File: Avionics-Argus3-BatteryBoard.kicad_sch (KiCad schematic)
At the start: 6 parts

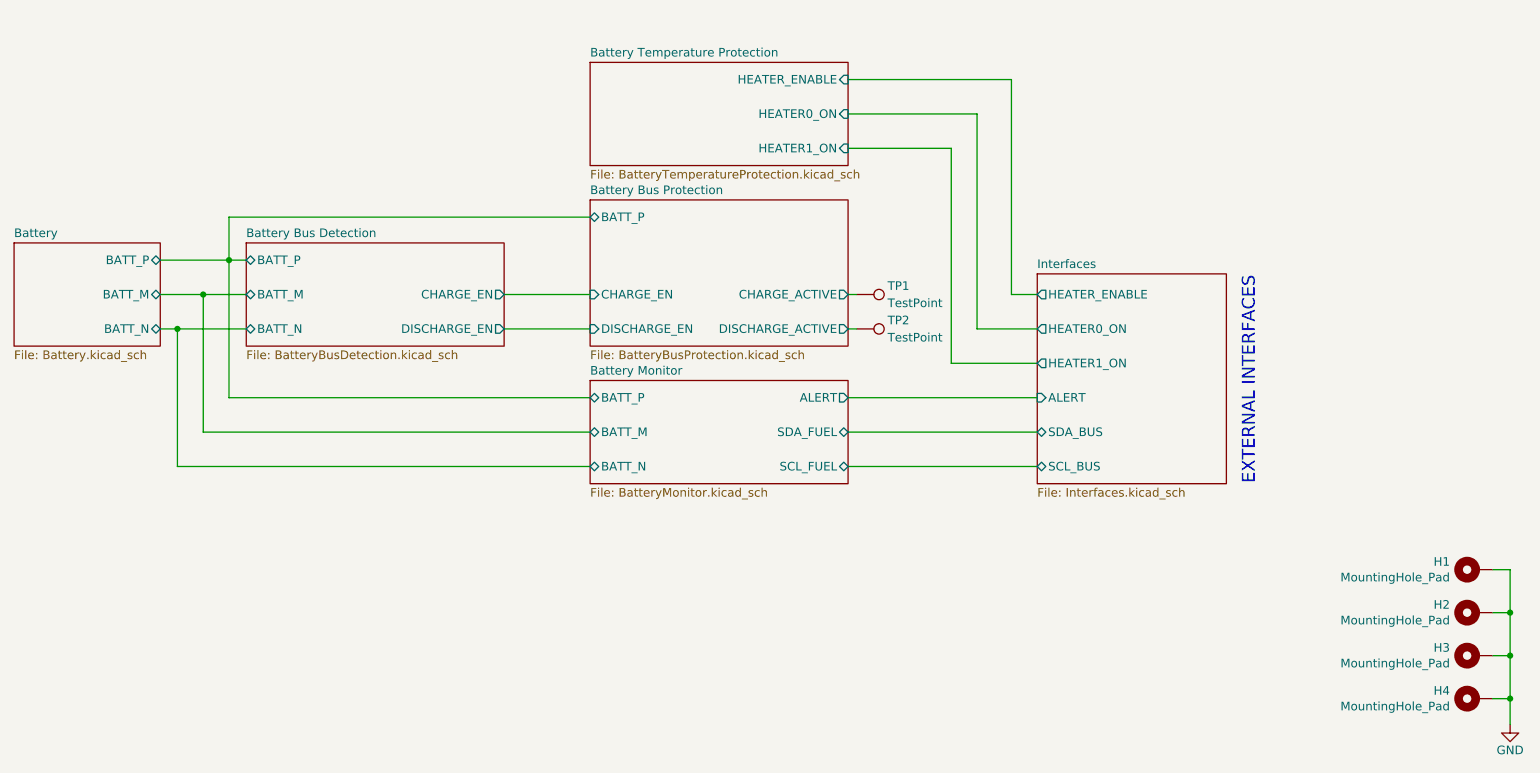
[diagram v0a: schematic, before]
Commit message: Updated Interface to MCU_Subsystem
removed old interface, added STM32U375CE with minimum design components for our operation. Still need to find voltage converter from BATT_P to 3.3v.
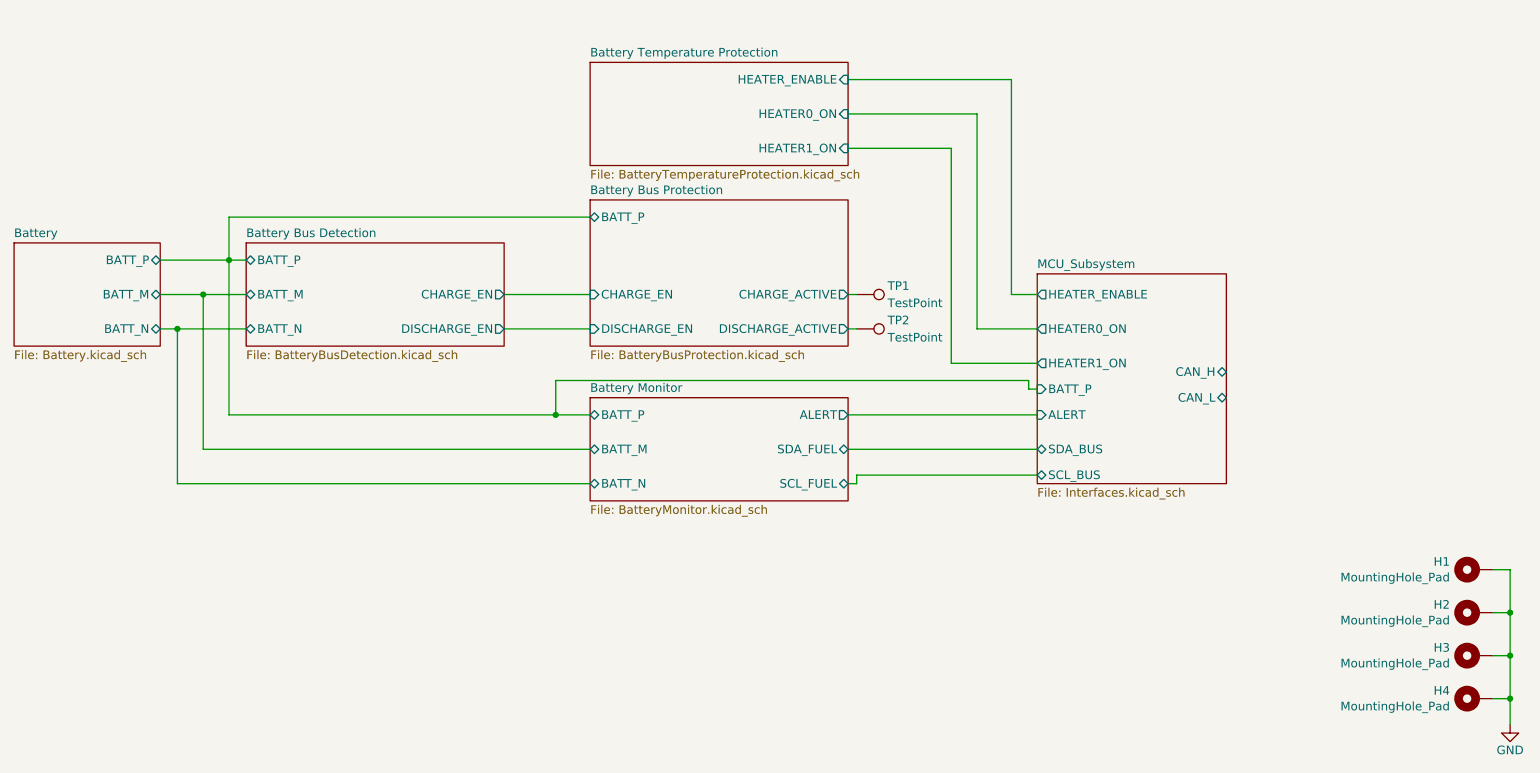
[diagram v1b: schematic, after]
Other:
- sheet Interfaces renamed MCU_Subsystem
- sheet MCU_Subsystem ports: added BATT_P, CAN_H, CAN_L; removed none
- note removed: "EXTERNAL INTERFACES"
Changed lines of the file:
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@@
 		(comment 3 "V. Rajesh")
-	)
-	(text "EXTERNAL INTERFACES"
-		(exclude_from_sim no)
-		(at 216.662 106.68 90)
-		(effects
-			(font
-				(size 1.905 1.905)
-			)
-		)
 	)
 	(junction
@@
 	)
 	(junction
+		(at 114.3 111.76)
+		(diameter 0)
+		(color 0 0 0 0)
+	)
+	(junction
 		(at 62.23 93.98)
 		(diameter 0)
@@
 	(wire
 		(pts
-			(xy 58.42 99.06) (xy 58.42 119.38)
+			(xy 58.42 99.06) (xy 58.42 121.92)
+		)
+		(stroke
+			(width 0)
+			(type default)
+		)
+	)
+	(wire
+		(pts
+			(xy 157.48 116.84) (xy 185.42 116.84)
 		)
 		(stroke
@@
 	(wire
 		(pts
+			(xy 157.48 111.76) (xy 185.42 111.76)
+		)
+		(stroke
+			(width 0)
+			(type default)
+		)
+	)
+	(wire
+		(pts
 			(xy 66.04 82.55) (xy 119.38 82.55)
 		)
@@
 	(wire
 		(pts
-			(xy 62.23 114.3) (xy 119.38 114.3)
+			(xy 62.23 116.84) (xy 119.38 116.84)
 		)
 		(stroke
@@
 	(wire
 		(pts
+			(xy 184.15 107.95) (xy 185.42 107.95)
+		)
+		(stroke
+			(width 0)
+			(type default)
+		)
+	)
+	(wire
+		(pts
 			(xy 106.68 99.06) (xy 119.38 99.06)
 		)
@@
 	(wire
 		(pts
+			(xy 158.75 120.65) (xy 185.42 120.65)
+		)
+		(stroke
+			(width 0)
+			(type default)
+		)
+	)
+	(wire
+		(pts
 			(xy 157.48 99.06) (xy 158.75 99.06)
 		)
@@
 	(wire
 		(pts
+			(xy 114.3 106.68) (xy 114.3 111.76)
+		)
+		(stroke
+			(width 0)
+			(type default)
+		)
+	)
+	(wire
+		(pts
+			(xy 184.15 106.68) (xy 114.3 106.68)
+		)
+		(stroke
+			(width 0)
+			(type default)
+		)
+	)
+	(wire
+		(pts
 			(xy 255.27 147.32) (xy 255.27 153.67)
 		)
@@
 	(wire
 		(pts
-			(xy 157.48 109.22) (xy 185.42 109.22)
-		)
-		(stroke
-			(width 0)
-			(type default)
-		)
-	)
-	(wire
-		(pts
 			(xy 157.48 67.31) (xy 176.53 67.31)
 		)
@@
 	(wire
 		(pts
-			(xy 157.48 114.3) (xy 185.42 114.3)
+			(xy 184.15 107.95) (xy 184.15 106.68)
 		)
 		(stroke
@@
 	(wire
 		(pts
-			(xy 119.38 109.22) (xy 66.04 109.22)
+			(xy 119.38 111.76) (xy 114.3 111.76)
 		)
 		(stroke
@@
 	(wire
 		(pts
-			(xy 66.04 88.9) (xy 66.04 109.22)
+			(xy 66.04 88.9) (xy 66.04 111.76)
 		)
 		(stroke
@@
 	(wire
 		(pts
-			(xy 157.48 119.38) (xy 185.42 119.38)
+			(xy 157.48 121.92) (xy 158.75 121.92)
 		)
 		(stroke
@@
 	(wire
 		(pts
-			(xy 62.23 93.98) (xy 62.23 114.3)
+			(xy 62.23 93.98) (xy 62.23 116.84)
 		)
 		(stroke
@@
 	(wire
 		(pts
+			(xy 158.75 121.92) (xy 158.75 120.65)
+		)
+		(stroke
+			(width 0)
+			(type default)
+		)
+	)
+	(wire
+		(pts
+			(xy 114.3 111.76) (xy 66.04 111.76)
+		)
+		(stroke
+			(width 0)
+			(type default)
+		)
+	)
+	(wire
+		(pts
 			(xy 157.48 93.98) (xy 158.75 93.98)
 		)
@@
 	(wire
 		(pts
-			(xy 119.38 119.38) (xy 58.42 119.38)
+			(xy 119.38 121.92) (xy 58.42 121.92)
 		)
 		(stroke
@@
 		)
 		(instances
-			(project "Avionics-BatteryBoard"
+			(project "Avionics-Argus3-BatteryBoard"
 				(path "/b6fd875d-6e05-4440-9a05-0f0aa046a0ef"
 					(page "4")
@@
 		)
 		(instances
-			(project "Avionics-BatteryBoard"
+			(project "Avionics-Argus3-BatteryBoard"
 				(path "/b6fd875d-6e05-4440-9a05-0f0aa046a0ef"
 					(page "2")
@@
 		)
 		(instances
-			(project "Avionics-BatteryBoard"
+			(project "Avionics-Argus3-BatteryBoard"
 				(path "/b6fd875d-6e05-4440-9a05-0f0aa046a0ef"
 					(page "6")
@@
 		)
 		(instances
-			(project "Avionics-BatteryBoard"
+			(project "Avionics-Argus3-BatteryBoard"
 				(path "/b6fd875d-6e05-4440-9a05-0f0aa046a0ef"
 					(page "11")
@@
 	)
 	(sheet
-		(at 119.38 106.68)
+		(at 119.38 109.22)
 		(size 38.1 15.24)
 		(exclude_from_sim no)
@@
 		)
 		(property "Sheetname" "Battery Monitor"
-			(at 119.38 105.9684 0)
+			(at 119.38 108.5084 0)
 			(effects
 				(font
@@
 		)
 		(property "Sheetfile" "BatteryMonitor.kicad_sch"
-			(at 119.38 122.5046 0)
+			(at 119.38 125.0446 0)
 			(effects
 				(font
@@
 		)
 		(pin "SDA_FUEL" bidirectional
-			(at 157.48 114.3 0)
+			(at 157.48 116.84 0)
 			(effects
 				(font
@@
 		)
 		(pin "SCL_FUEL" bidirectional
-			(at 157.48 119.38 0)
+			(at 157.48 121.92 0)
 			(effects
 				(font
@@
 		)
 		(pin "ALERT" output
-			(at 157.48 109.22 0)
+			(at 157.48 111.76 0)
 			(effects
 				(font
@@
 		)
 		(pin "BATT_M" bidirectional
-			(at 119.38 114.3 180)
+			(at 119.38 116.84 180)
 			(effects
 				(font
@@
 		)
 		(pin "BATT_N" bidirectional
-			(at 119.38 119.38 180)
+			(at 119.38 121.92 180)
 			(effects
 				(font
@@
 		)
 		(pin "BATT_P" bidirectional
-			(at 119.38 109.22 180)
+			(at 119.38 111.76 180)
 			(effects
 				(font
@@
 		)
 		(instances
-			(project "Avionics-BatteryBoard"
+			(project "Avionics-Argus3-BatteryBoard"
 				(path "/b6fd875d-6e05-4440-9a05-0f0aa046a0ef"
 					(page "3")
@@
 			(color 0 0 0 0.0000)
 		)
-		(property "Sheetname" "Interfaces"
+		(property "Sheetname" "MCU_Subsystem"
 			(at 185.42 90.2204 0)
 			(effects
@@
 		)
 		(pin "SDA_BUS" bidirectional
-			(at 185.42 114.3 180)
+			(at 185.42 116.84 180)
 			(effects
 				(font
@@
 		)
 		(pin "SCL_BUS" bidirectional
-			(at 185.42 119.38 180)
+			(at 185.42 120.65 180)
 			(effects
 				(font
@@
 		)
 		(pin "ALERT" input
-			(at 185.42 109.22 180)
+			(at 185.42 111.76 180)
 			(effects
 				(font
@@
 			)
 		)
+		(pin "CAN_L" bidirectional
+			(at 213.36 109.22 0)
+			(effects
+				(font
+					(size 1.27 1.27)
+				)
+				(justify right)
+			)
+		)
+		(pin "BATT_P" input
+			(at 185.42 107.95 180)
+			(effects
+				(font
+					(size 1.27 1.27)
+				)
+				(justify left)
+			)
+		)
+		(pin "CAN_H" bidirectional
+			(at 213.36 105.41 0)
+			(effects
+				(font
+					(size 1.27 1.27)
+				)
+				(justify right)
+			)
+		)
 		(instances
-			(project "Avionics-BatteryBoard"
+			(project "Avionics-Argus3-BatteryBoard"
 				(path "/b6fd875d-6e05-4440-9a05-0f0aa046a0ef"
 					(page "10")

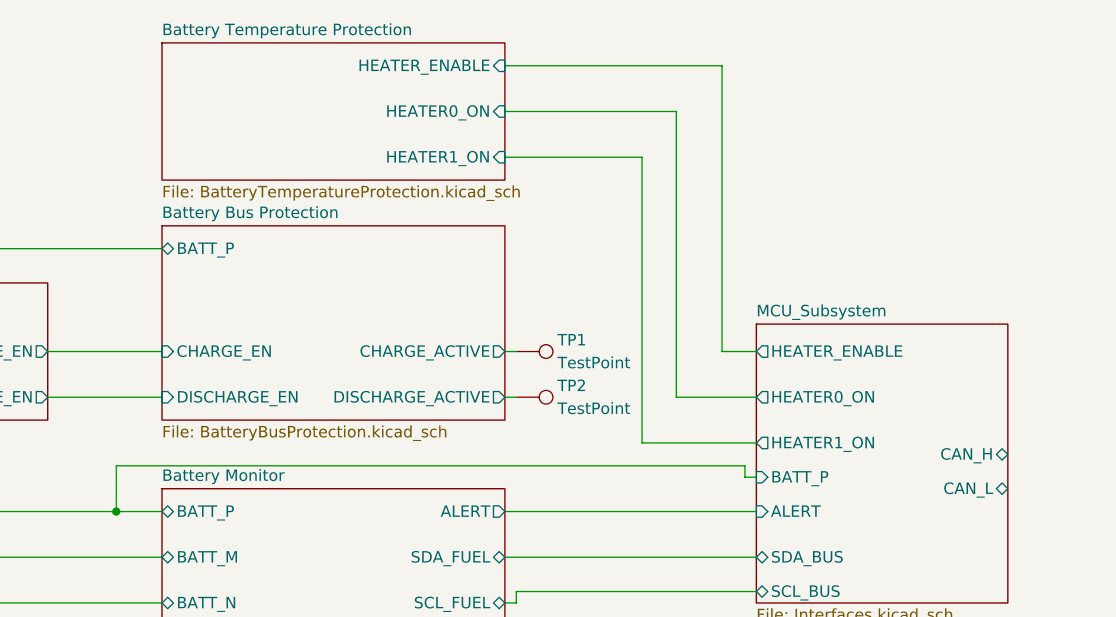
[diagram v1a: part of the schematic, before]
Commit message: Replaced old Interfaces with MCU
Added STM32U375CET6 mcu to board controlling the heaters and charging based on fuel gauge output.

Uses CAN for communication with mainboard.
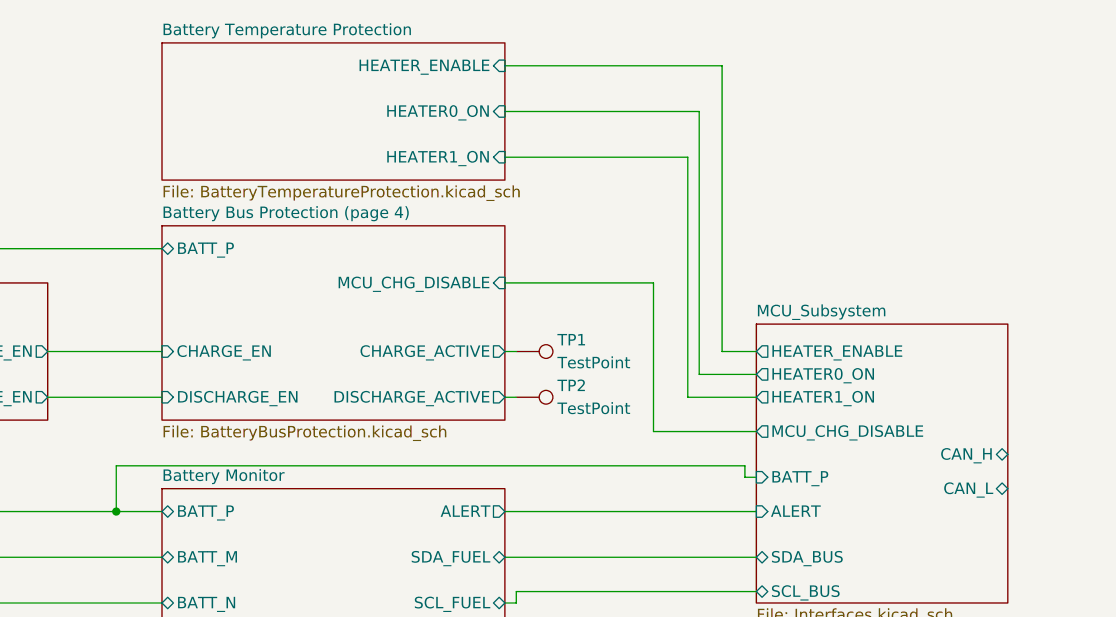
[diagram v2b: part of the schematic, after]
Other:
- sheet Battery Bus Protection renamed Battery Bus Protection (page 4)
- sheet Battery Bus Protection (page 4) ports: added MCU_CHG_DISABLE; removed none
- sheet MCU_Subsystem ports: added MCU_CHG_DISABLE; removed none
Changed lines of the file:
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@@
 	(wire
 		(pts
-			(xy 176.53 99.06) (xy 185.42 99.06)
+			(xy 179.07 96.52) (xy 185.42 96.52)
 		)
 		(stroke
@@
 	(wire
 		(pts
-			(xy 172.72 104.14) (xy 172.72 72.39)
+			(xy 177.8 99.06) (xy 177.8 72.39)
 		)
 		(stroke
@@
 	(wire
 		(pts
+			(xy 173.99 102.87) (xy 173.99 86.36)
+		)
+		(stroke
+			(width 0)
+			(type default)
+		)
+	)
+	(wire
+		(pts
 			(xy 55.88 93.98) (xy 62.23 93.98)
 		)
@@
 	(wire
 		(pts
-			(xy 157.48 67.31) (xy 176.53 67.31)
+			(xy 173.99 86.36) (xy 157.48 86.36)
+		)
+		(stroke
+			(width 0)
+			(type default)
+		)
+	)
+	(wire
+		(pts
+			(xy 157.48 67.31) (xy 179.07 67.31)
 		)
 		(stroke
@@
 	(wire
 		(pts
-			(xy 185.42 104.14) (xy 172.72 104.14)
+			(xy 185.42 102.87) (xy 173.99 102.87)
+		)
+		(stroke
+			(width 0)
+			(type default)
+		)
+	)
+	(wire
+		(pts
+			(xy 185.42 99.06) (xy 177.8 99.06)
 		)
 		(stroke
@@
 	(wire
 		(pts
-			(xy 157.48 72.39) (xy 172.72 72.39)
+			(xy 157.48 72.39) (xy 177.8 72.39)
 		)
 		(stroke
@@
 	(wire
 		(pts
-			(xy 176.53 67.31) (xy 176.53 99.06)
+			(xy 179.07 67.31) (xy 179.07 96.52)
 		)
 		(stroke
@@
 			(color 0 0 0 0.0000)
 		)
-		(property "Sheetname" "Battery Bus Protection"
+		(property "Sheetname" "Battery Bus Protection (page 4)"
 			(at 119.38 79.2984 0)
 			(effects
@@
 				)
 				(justify left)
+			)
+		)
+		(pin "MCU_CHG_DISABLE" input
+			(at 157.48 86.36 0)
+			(effects
+				(font
+					(size 1.27 1.27)
+				)
+				(justify right)
 			)
 		)
@@
 		)
 		(pin "HEATER1_ON" output
-			(at 185.42 104.14 180)
+			(at 185.42 99.06 180)
 			(effects
 				(font
@@
 		)
 		(pin "HEATER0_ON" output
-			(at 185.42 99.06 180)
+			(at 185.42 96.52 180)
 			(effects
 				(font
@@
 			)
 		)
+		(pin "MCU_CHG_DISABLE" output
+			(at 185.42 102.87 180)
+			(effects
+				(font
+					(size 1.27 1.27)
+				)
+				(justify left)
+			)
+		)

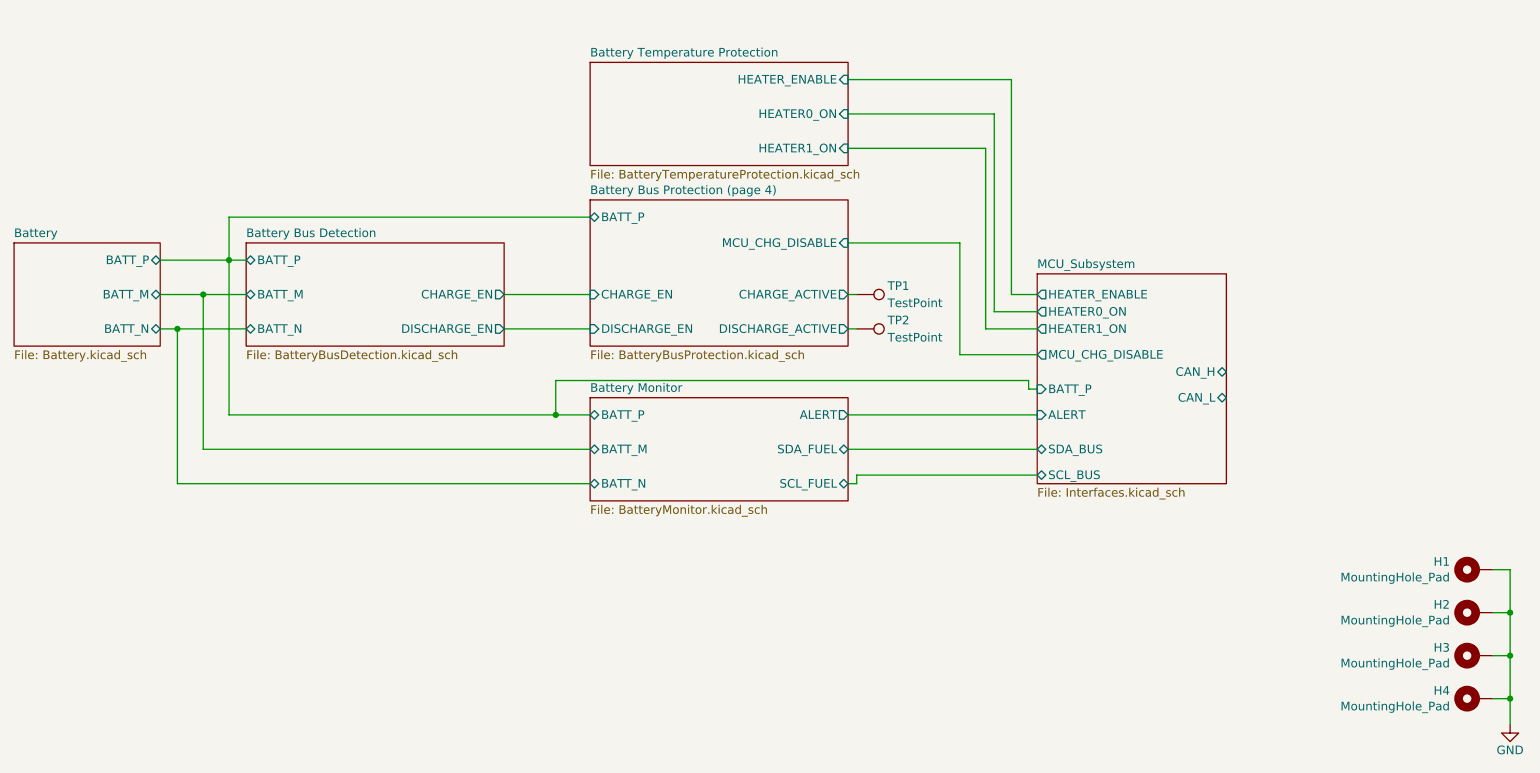
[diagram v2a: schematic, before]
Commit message: Added Schmitt Trigger mode for heaters
In the event that the mcu goes down, the thermistors will now be ale to control the heaters independently.
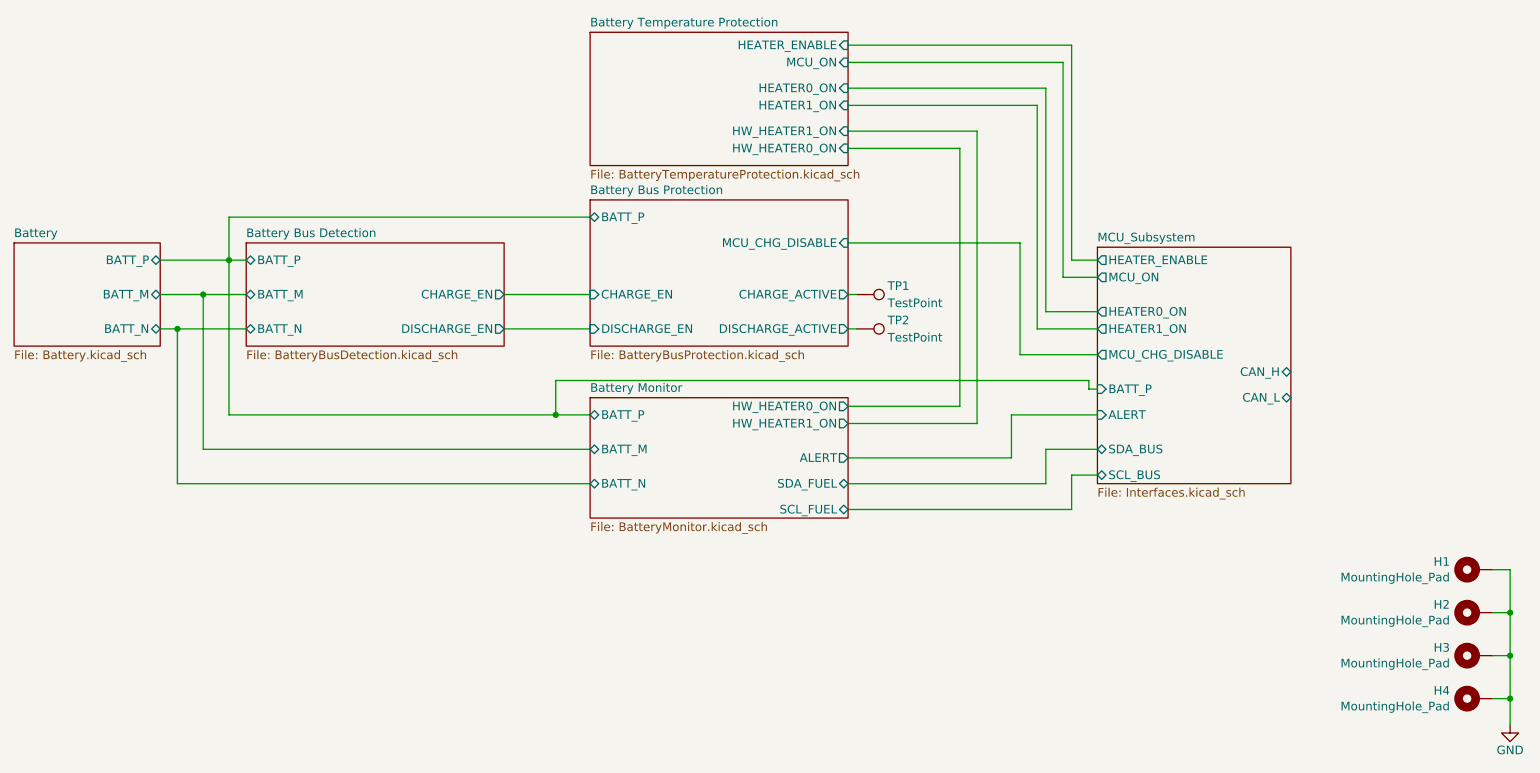
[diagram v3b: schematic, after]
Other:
- sheet Battery Bus Protection (page 4) renamed Battery Bus Protection
- sheet Battery Monitor ports: added HW_HEATER0_ON, HW_HEATER1_ON; removed none
- sheet Battery Temperature Protection ports: added HW_HEATER0_ON, HW_HEATER1_ON, MCU_ON; removed none
- sheet MCU_Subsystem ports: added MCU_ON; removed none

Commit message: finished layout
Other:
- sheet MCU_Subsystem ports: added CAN_N, CAN_P; removed CAN_H, CAN_L
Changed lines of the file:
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@@
 			)
 		)
-		(pin "CAN_L" bidirectional
+		(pin "CAN_N" bidirectional
 			(at 222.885 109.22 0)
 			(effects
@@
 			)
 		)
-		(pin "CAN_H" bidirectional
+		(pin "CAN_P" bidirectional
 			(at 222.885 105.41 0)
 			(effects
